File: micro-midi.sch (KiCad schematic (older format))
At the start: 18 parts, among them J1 AudioJack3, J2 Conn_01x04_Male, J3 AudioJack3, U1 74HC04, U2 6N137

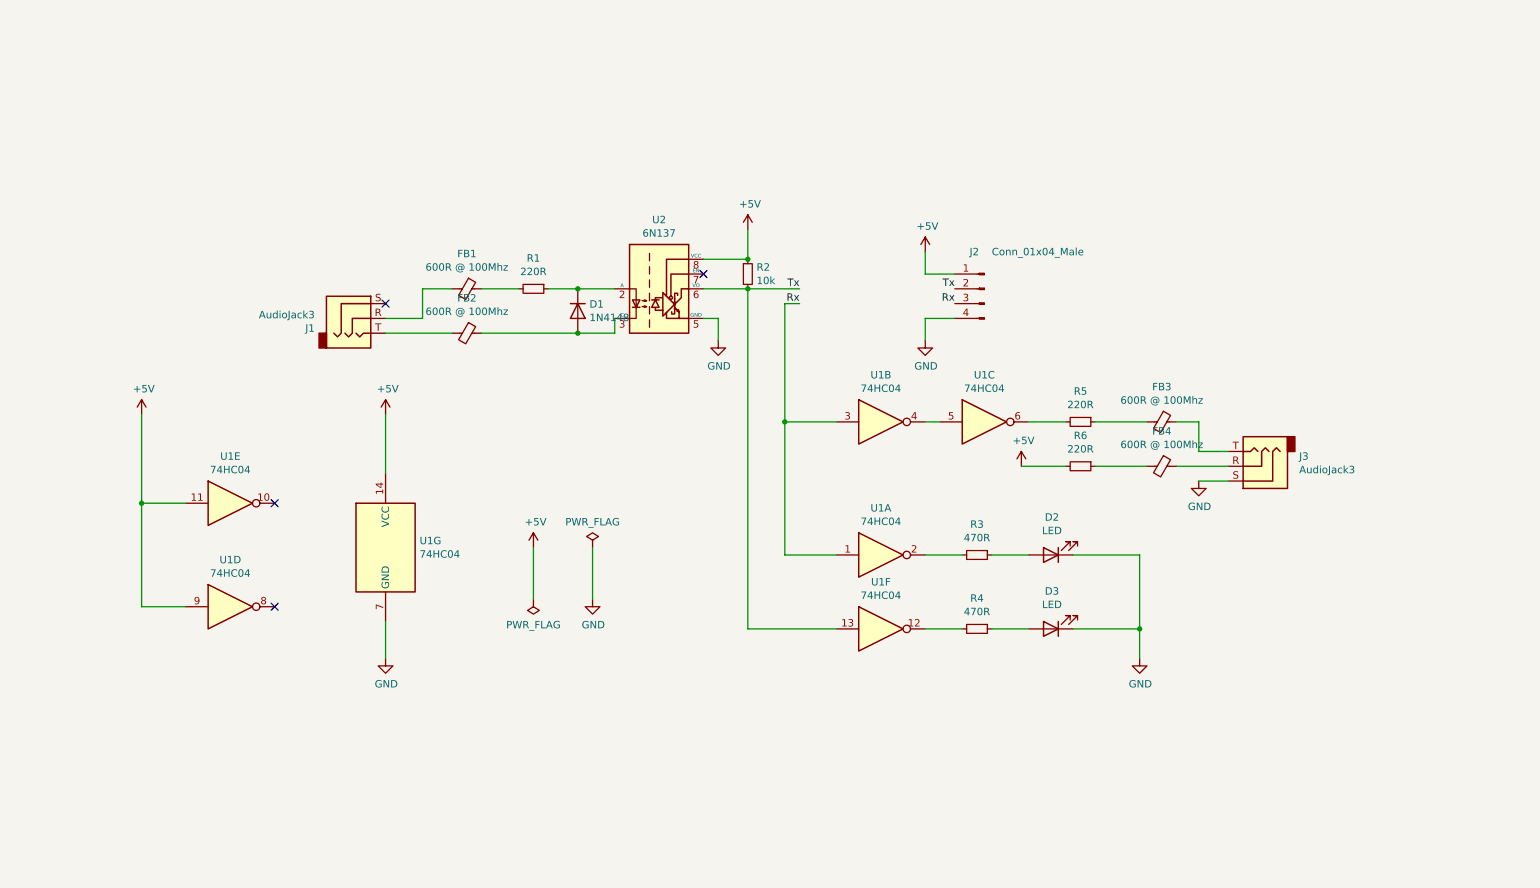
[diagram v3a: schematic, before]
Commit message: split schematics for input and output
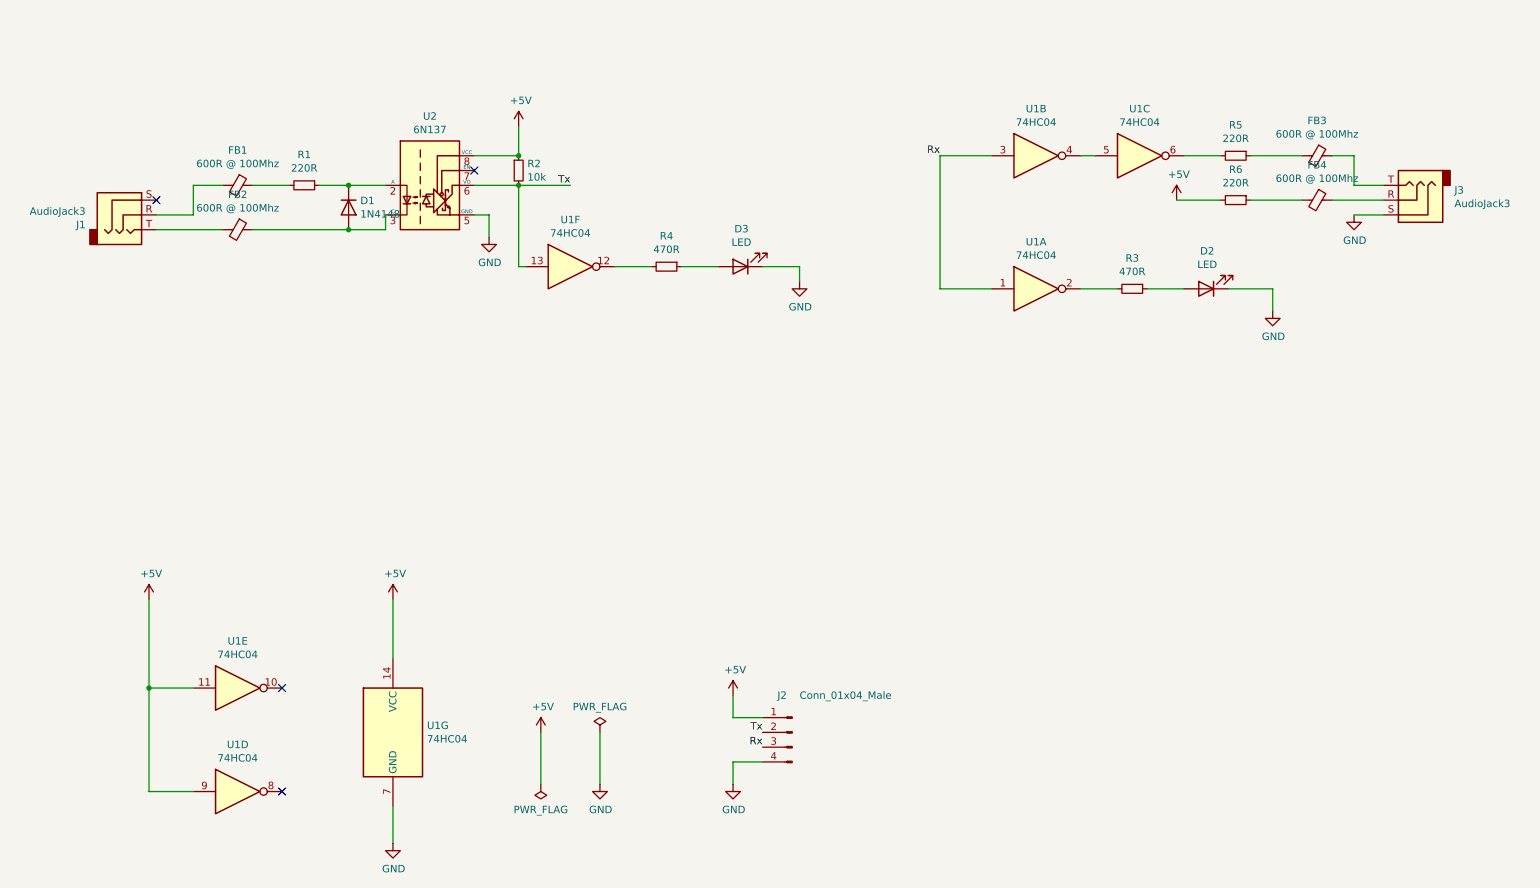
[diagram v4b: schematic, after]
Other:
- moved on the sheet: D1, D2, D3, FB1, FB2, FB3, FB4, J1, J2, J3, R1, R2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
